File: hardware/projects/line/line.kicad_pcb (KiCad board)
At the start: 2 copper layers, 7.5 x 15 mm, 5 parts, among them J1 Conn_01x03, U1 QRE1113GR

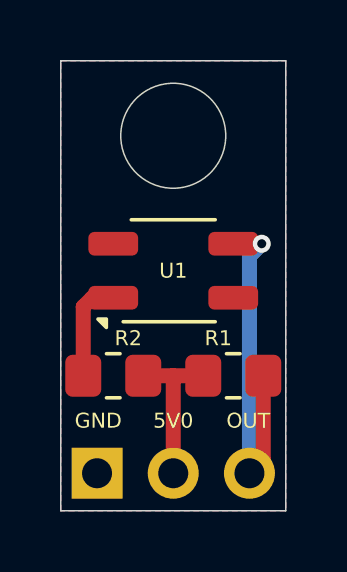
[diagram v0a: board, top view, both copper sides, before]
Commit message: chore: remove 3D body of line sensor
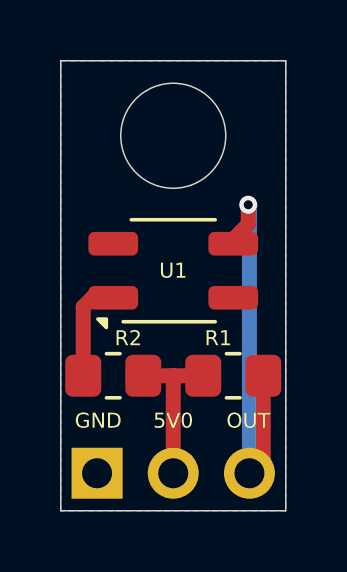
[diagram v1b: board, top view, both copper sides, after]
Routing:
- net /OUT: track 12.2 -> 13.9 mm
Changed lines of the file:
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@@
 				(font
 					(size 0.5 0.5)
-					(thickness 0.15)
+					(thickness 0.125)
 				)
 			)
@@
 		)
 		(embedded_fonts no)
-		(model "${KICAD10_3DMODEL_DIR}/Connector_PinHeader_2.54mm.3dshapes/PinHeader_1x03_P2.54mm_Vertical.step"
-			(offset
-				(xyz 0 0 0)
-			)
-			(scale
-				(xyz 1 1 1)
-			)
-			(rotate
-				(xyz 0 0 0)
-			)
-		)
 	)
 	(footprint "OptoDevice:OnSemi_CASE100CY"
@@
 	)
 	(segment
+		(start 148.75 107.45)
+		(end 148.25 107.95)
+		(width 0.5)
+		(layer "F.Cu")
+		(net "/OUT")
+	)
+	(segment
+		(start 148.25 107.95)
+		(end 148.25 108.1)
+		(width 0.5)
+		(layer "F.Cu")
+		(net "/OUT")
+	)
+	(segment
 		(start 149.25 115.29)
 		(end 149.25 112.5)
@@
 	)
 	(segment
-		(start 148.25 108.1)
-		(end 149.2 108.1)
+		(start 148.75 106.8)
+		(end 148.75 107.45)
 		(width 0.5)
 		(layer "F.Cu")
@@
 	)
 	(via
-		(at 149.2 108.1)
+		(at 148.75 106.8)
 		(size 0.6)
 		(drill 0.3)
@@
 	)
 	(segment
-		(start 148.79 108.51)
+		(start 148.75 106.8)
+		(end 148.79 106.84)
+		(width 0.5)
+		(layer "B.Cu")
+		(net "/OUT")
+	)
+	(segment
+		(start 148.79 106.84)
 		(end 148.79 115.75)
 		(width 0.5)
 		(layer "B.Cu")
-		(net "/OUT")
-	)
-	(segment
-		(start 149.2 108.1)
-		(end 148.79 108.51)
-		(width 0.5)
-		(layer "B.Cu")

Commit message: fix: line sensor dimensions
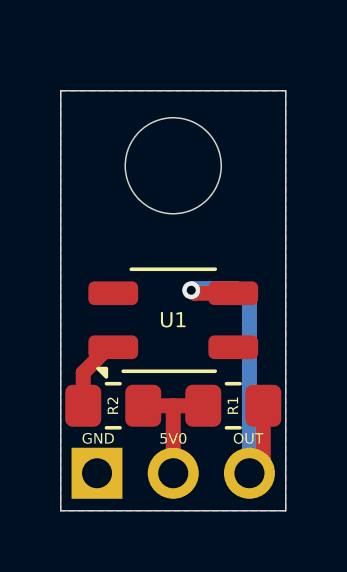
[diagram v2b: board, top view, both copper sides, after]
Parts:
- moved G*** 2.75 mm to (146.2, 111.8)
- moved U1 1.65 mm to (146.2, 110.7)
- moved R1 1.00 mm to (148.2, 113.5)
- moved R2 1.00 mm to (144.2, 113.5)
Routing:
- net /OUT: track 13.9 -> 11.7 mm
- net +5V: track 5.25 -> 4.25 mm
- net /DIODE: track 3.42 -> 2.45 mm
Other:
- board size 7.5 x 15 mm -> 7.5 x 14 mm
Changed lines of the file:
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@@
 	(footprint "Resistor_SMD:R_0805_2012Metric_Pad1.20x1.40mm_HandSolder"
 		(layer "F.Cu")
-		(at 144.25 112.5 180)
+		(at 144.25 113.5 180)
 		(descr "Resistor SMD 0805 (2012 Metric), square (rectangular) end terminal, IPC-7351 nominal with elongated pad for handsoldering. (Body size source: IPC-SM-782 page 72, https://www.pcb-3d.com/wordpress/wp-content/uploads/ipc-sm-782a_amendment_1_and_2.pdf)")
 		(tags "resistor handsolder")
 		(property "Reference" "R2"
-			(at -0.5 1.25 0)
+			(at 0 0 90)
 			(layer "F.SilkS")
 			(effects
 				(font
-					(size 0.5 0.5)
+					(size 0.35 0.35)
 					(thickness 0.15)
 				)
@@
 		(duplicate_pad_numbers_are_jumpers no)
 		(fp_rect
-			(start -1.77 -1.77)
-			(end 1.77 6.85)
+			(start -1.25 -1.25)
+			(end 1.25 6.35)
 			(stroke
 				(width 0.05)
@@
 			(pinfunction "Pin_1_1")
 			(pintype "passive")
+			(zone_connect 2)
 		)
 		(pad "2" thru_hole circle
@@
 	(footprint "OptoDevice:OnSemi_CASE100CY"
 		(layer "F.Cu")
-		(at 146.25 109 90)
+		(at 146.25 110.65 90)
 		(descr "OnSemi CASE 100CY, light-direction upwards, see http://www.onsemi.com/pub/Collateral/QRE1113-D.PDF")
 		(tags "refective opto couple photo coupler")
@@
 	(footprint "Resistor_SMD:R_0805_2012Metric_Pad1.20x1.40mm_HandSolder"
 		(layer "F.Cu")
-		(at 148.25 112.5)
+		(at 148.25 113.5)
 		(descr "Resistor SMD 0805 (2012 Metric), square (rectangular) end terminal, IPC-7351 nominal with elongated pad for handsoldering. (Body size source: IPC-SM-782 page 72, https://www.pcb-3d.com/wordpress/wp-content/uploads/ipc-sm-782a_amendment_1_and_2.pdf)")
 		(tags "resistor handsolder")
 		(property "Reference" "R1"
-			(at -0.5 -1.25 0)
+			(at 0 0 90)
 			(layer "F.SilkS")
 			(effects
 				(font
-					(size 0.5 0.5)
+					(size 0.35 0.35)
 					(thickness 0.15)
 				)
@@
 	(footprint "dolphin:LOGO_Gengar_05MM"
 		(layer "B.Cu")
-		(at 146.25 109 180)
+		(at 146.25 111.75 180)
 		(descr "Equipe Paralela 10mm mascot")
 		(property "Reference" "G***"
@@
 	)
 	(gr_line
-		(start 142.5 102)
+		(start 142.5 103)
 		(end 142.5 117)
 		(stroke
@@
 	)
 	(gr_line
-		(start 142.5 102)
-		(end 150 102)
+		(start 142.5 103)
+		(end 150 103)
 		(stroke
 			(width 0.05)
@@
 	)
 	(gr_circle
-		(center 146.25 104.5)
-		(end 148 104.5)
+		(center 146.25 105.5)
+		(end 147.85 105.5)
 		(stroke
 			(width 0.05)
@@
 	)
 	(gr_line
-		(start 150 102)
+		(start 150 103)
 		(end 150 117)
 		(stroke
@@
 	)
 	(gr_text "GND"
-		(at 143.75 114 0)
+		(at 143.75 114.6 0)
 		(layer "F.SilkS")
 		(effects
 			(font
-				(size 0.5 0.5)
+				(size 0.35 0.35)
 				(thickness 0.1)
 			)
@@
 	)
 	(gr_text "5V0"
-		(at 146.25 114 0)
+		(at 146.25 114.6 0)
 		(layer "F.SilkS")
 		(effects
 			(font
-				(size 0.5 0.5)
+				(size 0.35 0.35)
 				(thickness 0.1)
 			)
@@
 	)
 	(gr_text "OUT"
-		(at 148.75 114 0)
+		(at 148.75 114.6 0)
 		(layer "F.SilkS")
 		(effects
 			(font
-				(size 0.5 0.5)
+				(size 0.35 0.35)
 				(thickness 0.1)
 			)
@@
 	)
 	(gr_text "GND"
-		(at 143.75 114 0)
+		(at 143.75 114.6 0)
 		(layer "B.SilkS")
 		(effects
 			(font
-				(size 0.5 0.5)
+				(size 0.35 0.35)
 				(thickness 0.1)
 			)
@@
 	)
 	(gr_text "5V0"
-		(at 146.25 114 0)
+		(at 146.25 114.6 0)
 		(layer "B.SilkS")
 		(effects
 			(font
-				(size 0.5 0.5)
+				(size 0.35 0.35)
 				(thickness 0.1)
 			)
@@
 	)
 	(gr_text "OUT"
-		(at 148.75 114 0)
+		(at 148.75 114.6 0)
 		(layer "B.SilkS")
 		(effects
 			(font
-				(size 0.5 0.5)
+				(size 0.35 0.35)
 				(thickness 0.1)
 			)
@@
 		(layer "Dwgs.User")
 		(pts
-			(xy 146.25 117) (xy 146.25 104.5)
+			(xy 142.5 117) (xy 146.25 105.5)
 		)
 		(height -12.5)
@@
 			(keep_text_aligned yes)
 		)
-		(gr_text "12,5"
-			(at 132.6 110.75 90)
+		(gr_text "11,5"
+			(at 128.85 111.25 90)
 			(layer "Dwgs.User")
 			(effects
@@
 		(layer "Dwgs.User")
 		(pts
-			(xy 150 117) (xy 150 102)
+			(xy 146.25 110.65) (xy 142.5 117)
+		)
+		(height -10)
+		(orientation 1)
+		(format
+			(prefix "")
+			(suffix "")
+			(units 3)
+			(units_format 0)
+			(precision 4)
+			(suppress_zeroes yes)
+		)
+		(style
+			(thickness 0.1)
+			(arrow_length 1.27)
+			(text_position_mode 0)
+			(arrow_direction outward)
+			(extension_height 0.58642)
+			(extension_offset 0.5)
+			(keep_text_aligned yes)
+		)
+		(gr_text "6,35"
+			(at 135.1 113.825 90)
+			(layer "Dwgs.User")
+			(effects
+				(font
+					(size 1 1)
+					(thickness 0.15)
+				)
+			)
+		)
+	)
+	(dimension
+		(type orthogonal)
+		(layer "Dwgs.User")
+		(pts
+			(xy 146.25 107.1) (xy 146.25 103.9)
+		)
+		(height 7.5)
+		(orientation 1)
+		(format
+			(prefix "")
+			(suffix "")
+			(units 3)
+			(units_format 0)
+			(precision 4)
+			(suppress_zeroes yes)
+		)
+		(style
+			(thickness 0.1)
+			(arrow_length 1.27)
+			(text_position_mode 0)
+			(arrow_direction outward)
+			(extension_height 0.58642)
+			(extension_offset 0.5)
+			(keep_text_aligned yes)
+		)
+		(gr_text "3,2"
+			(at 152.6 105.5 90)
+			(layer "Dwgs.User")
+			(effects
+				(font
+					(size 1 1)
+					(thickness 0.15)
+				)
+			)
+		)
+	)
+	(dimension
+		(type orthogonal)
+		(layer "Dwgs.User")
+		(pts
+			(xy 150 117) (xy 150 103)
 		)
 		(height 8.75)
@@
 			(keep_text_aligned yes)
 		)
-		(gr_text "15"
-			(at 157.6 109.5 90)
+		(gr_text "14"
+			(at 157.6 110 90)
 			(layer "Dwgs.User")
 			(effects
@@
 	(segment
 		(start 146.25 115.75)
-		(end 146.25 112.5)
+		(end 146.25 113.5)
 		(width 0.5)
 		(layer "F.Cu")
@@
 	)
 	(segment
-		(start 146.25 112.5)
-		(end 147.25 112.5)
+		(start 145.25 113.5)
+		(end 147.25 113.5)
 		(width 0.5)
 		(layer "F.Cu")
@@
 	)
 	(segment
-		(start 145.25 112.5)
-		(end 146.25 112.5)
-		(width 0.5)
-		(layer "F.Cu")
-		(net "+5V")
-	)
-	(segment
-		(start 143.25 110.2)
-		(end 143.25 112.5)
+		(start 144.1 111.55)
+		(end 143.25 112.4)
 		(width 0.5)
 		(layer "F.Cu")
@@
 	)
 	(segment
-		(start 144.25 109.9)
-		(end 143.55 109.9)
+		(start 144.25 111.55)
+		(end 144.1 111.55)
 		(width 0.5)
 		(layer "F.Cu")
@@
 	)
 	(segment
-		(start 143.55 109.9)
-		(end 143.25 110.2)
+		(start 143.25 112.4)
+		(end 143.25 113.5)
 		(width 0.5)
 		(layer "F.Cu")
 		(net "/DIODE")
+	)
+	(segment
+		(start 149.25 115.29)
+		(end 149.25 113.5)
+		(width 0.5)
+		(layer "F.Cu")
+		(net "/OUT")
+	)
+	(segment
+		(start 146.95 109.75)
+		(end 148.25 109.75)
+		(width 0.5)
+		(layer "F.Cu")
+		(net "/OUT")
+	)
+	(segment
+		(start 146.85 109.65)
+		(end 146.95 109.75)
+		(width 0.5)
+		(layer "F.Cu")
+		(net "/OUT")
 	)
 	(segment
@@
 		(net "/OUT")
 	)
-	(segment
-		(start 148.75 107.45)
-		(end 148.25 107.95)
-		(width 0.5)
-		(layer "F.Cu")
-		(net "/OUT")
-	)
-	(segment
-		(start 148.25 107.95)
-		(end 148.25 108.1)
-		(width 0.5)
-		(layer "F.Cu")
-		(net "/OUT")
-	)
-	(segment
-		(start 149.25 115.29)
-		(end 149.25 112.5)
-		(width 0.5)
-		(layer "F.Cu")
-		(net "/OUT")
-	)
-	(segment
-		(start 148.75 106.8)
-		(end 148.75 107.45)
-		(width 0.5)
-		(layer "F.Cu")
-		(net "/OUT")
-	)
 	(via
-		(at 148.75 106.8)
+		(at 146.85 109.65)
 		(size 0.6)
 		(drill 0.3)
@@
 	)
 	(segment
-		(start 148.75 106.8)
-		(end 148.79 106.84)
+		(start 146.85 109.65)
+		(end 146.9 109.6)
 		(width 0.5)
 		(layer "B.Cu")
@@
 	)
 	(segment
-		(start 148.79 106.84)
+		(start 148.79 110.04)
 		(end 148.79 115.75)
+		(width 0.5)
+		(layer "B.Cu")
+		(net "/OUT")
+	)
+	(segment
+		(start 148.35 109.6)
+		(end 148.79 110.04)
+		(width 0.5)
+		(layer "B.Cu")
+		(net "/OUT")
+	)
+	(segment
+		(start 146.9 109.6)
+		(end 148.35 109.6)
 		(width 0.5)
 		(layer "B.Cu")
@@
 		(polygon
 			(pts
-				(xy 150 117) (xy 142.5 117) (xy 142.5 102) (xy 150 102)
-			)
-		)
+				(xy 150 117) (xy 142.5 117) (xy 142.5 103) (xy 150 103)
+			)
+		)
